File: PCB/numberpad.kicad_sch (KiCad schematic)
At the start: 70 parts, among them J1 Light_Sensor, J2 Rotary_Encoder, J3 Screen_Connector, J4 FingerPrint_UART, J5 USB_A, J6 Programmer, J7 USB_C_TO_PC, SW0 0, SW1 ., SW10 8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

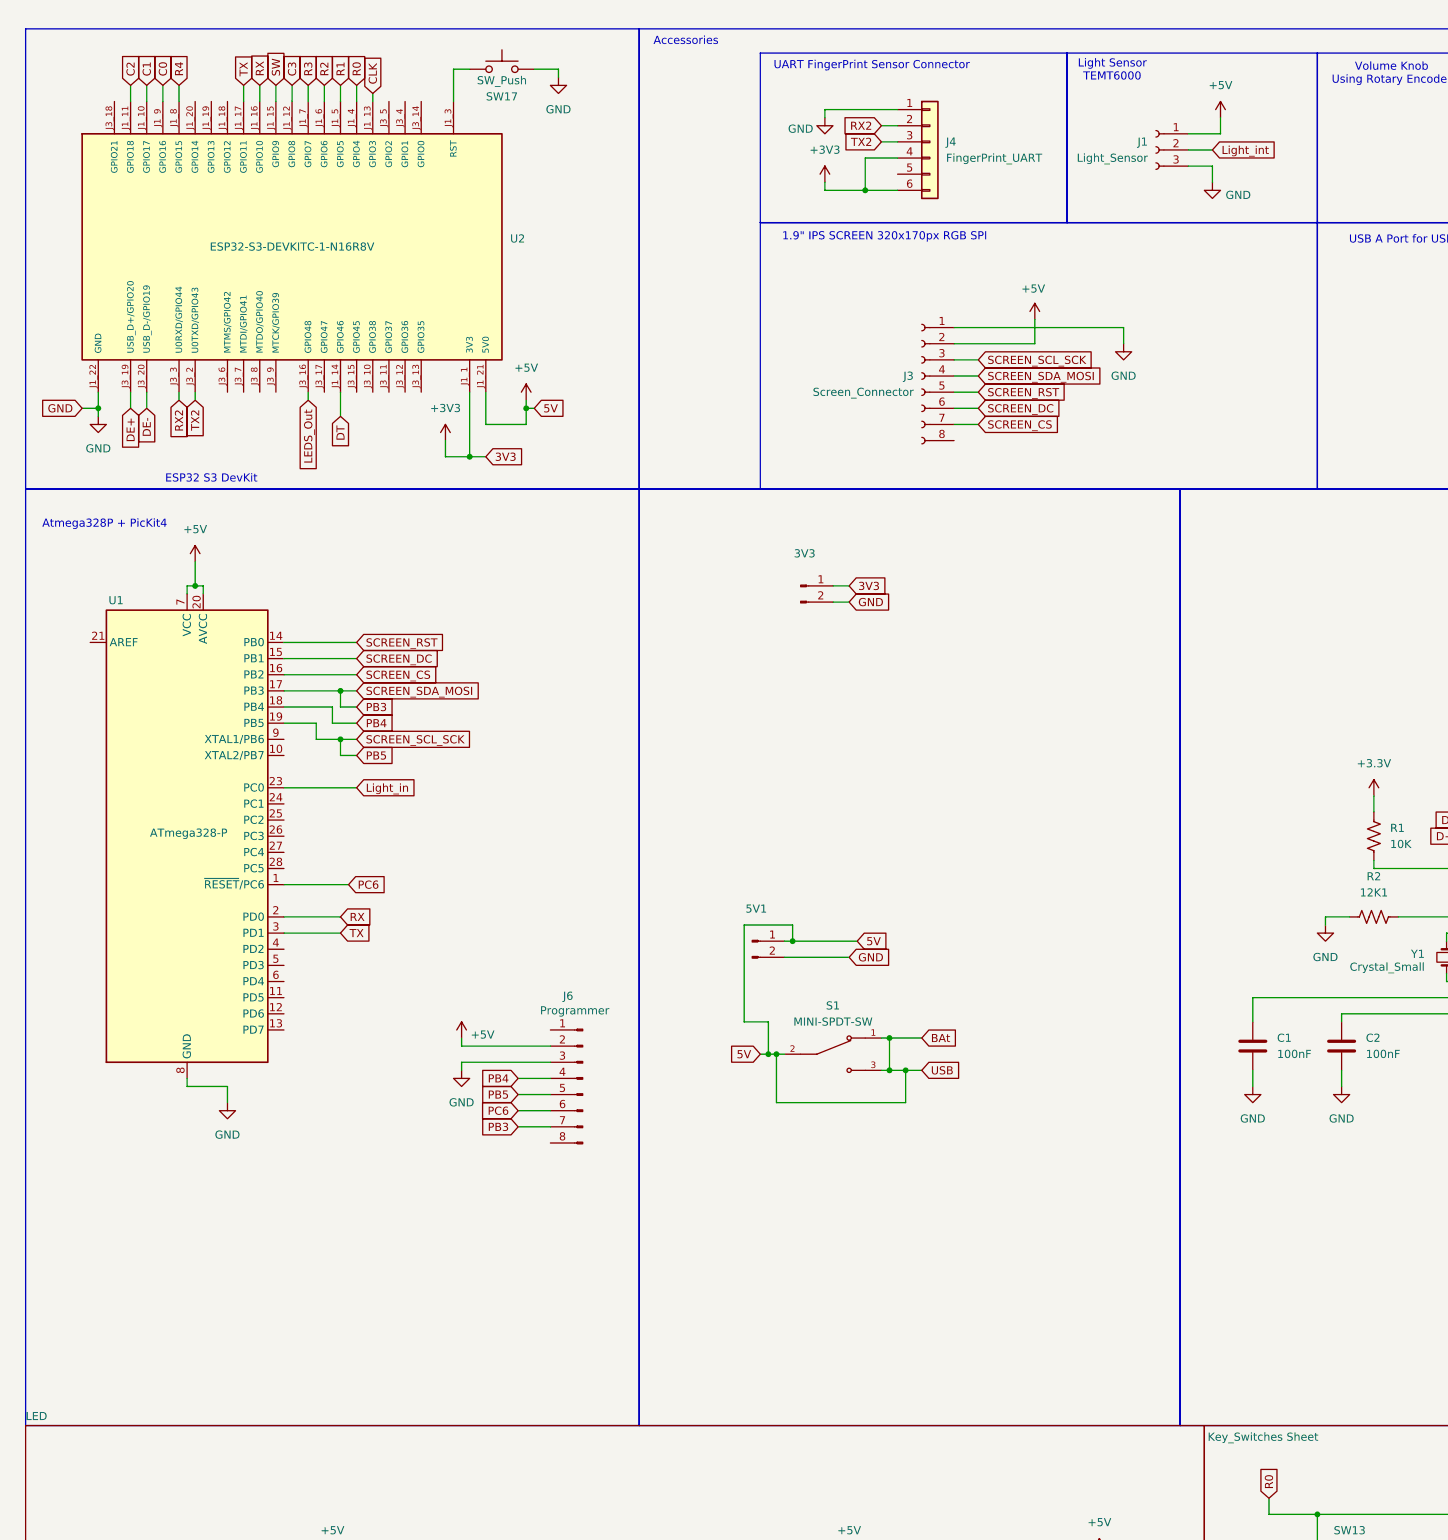
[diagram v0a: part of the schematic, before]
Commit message: v.1.1
PCB Key spacing, style refresh, web ui bug fix, qol feature implimentation (cart item ajust, remove from cart)
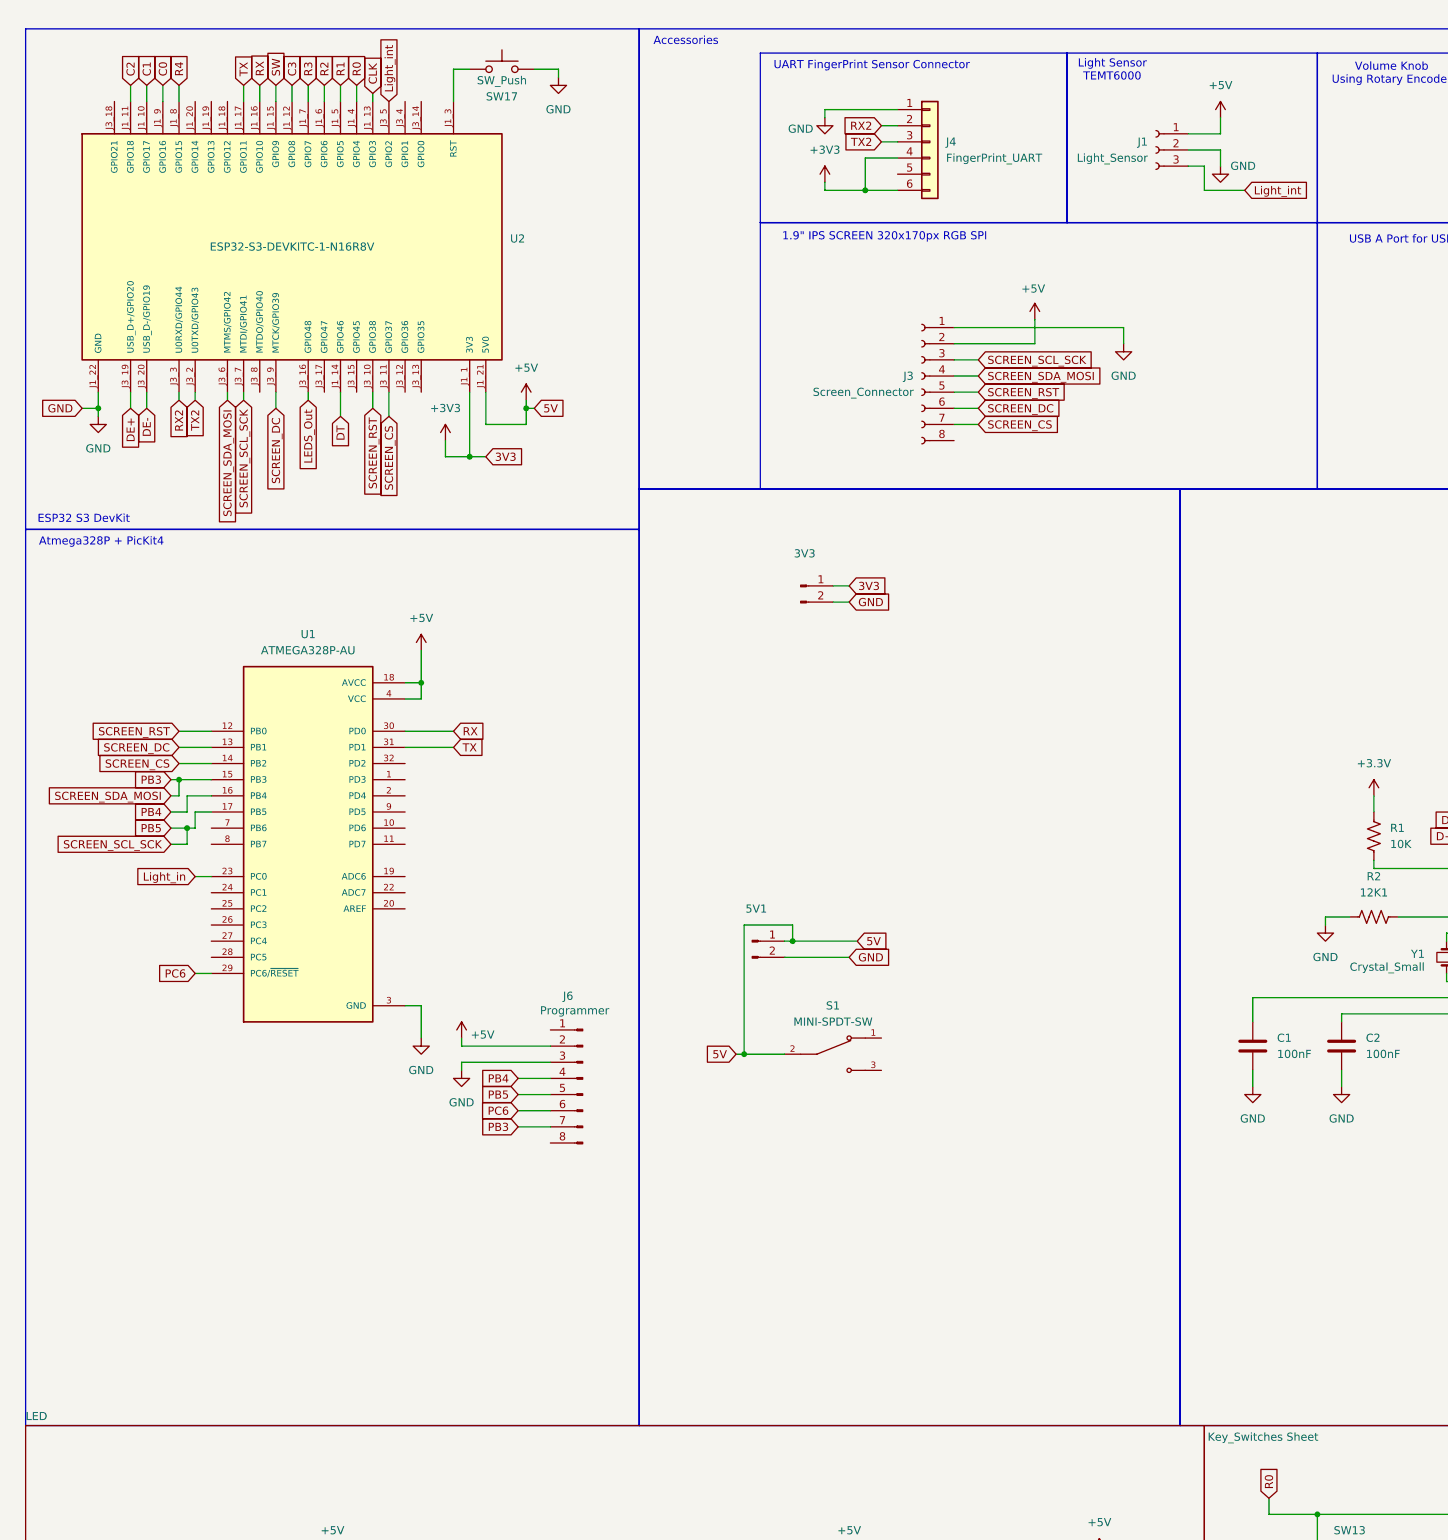
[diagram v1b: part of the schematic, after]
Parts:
- removed U1: ATmega328-P, footprints:QFP80P900X900X120-32N, symbol MCU_Microchip_ATmega:ATmega328-P
- added U1: ATMEGA328P-AU, footprints:QFP80P900X900X120-32N, symbol ATMEGA328P-AU:ATMEGA328P-AU
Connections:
- net +5V: now also U1.18 (AVCC), U1.4 (VCC), U1.6 (VCC); no longer S1.1, S1.3
- net GND: now also J1.2 (Pin_2), U1.21 (GND), U1.3 (GND), U1.5 (GND); no longer J1.3 (Pin_3)
- net Light_in: now also U1.23 (PC0)
- net Light_int: now also J1.3 (Pin_3), U2.J3_5 (GPIO2); no longer J1.2 (Pin_2)
- net PB3: now also U2.J3_6 (MTMS/GPIO42), U1.15 (PB3)
- net PB4: now also U1.16 (PB4)
- net PB5: now also U2.J3_7 (MTDI/GPIO41), U1.17 (PB5)
- net PC6: now also U1.29 (PC6/~{RESET})
- net RX: now also U1.30 (PD0)
- net SCREEN_CS: now also U2.J3_11 (GPIO37), U1.14 (PB2)
- net SCREEN_DC: now also U2.J3_9 (MTCK/GPIO39), U1.13 (PB1)
- net SCREEN_RST: now also U2.J3_10 (GPIO38), U1.12 (PB0)
- net TX: now also U1.31 (PD1)
